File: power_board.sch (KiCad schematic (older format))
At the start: 32 parts, among them CON1 MICROUSB, J1 Conn_02x03_Odd_Even, J2 Conn_01x01, J3 Conn_01x01, J4 Conn_01x01, SW1 SW_Push, U1 PCA9555PW, U2 ATMEGA328P-AU, U3 PCA9555PW, U4 FT232RL, Y1 Crystal

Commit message: Added capacitor references
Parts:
- C1, C10, C2, C5, C6, C7, C8, C9: manf# (none) -> EMK107B7104KAHT
- C3, C4: manf# (none) -> C0603C223K4RACTU
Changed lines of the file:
@@
 F 2 "lsts-passives:C_0603" H 7438 2550 50  0001 C CNN
 F 3 "~" H 7400 2700 50  0001 C CNN
+F 4 "EMK107B7104KAHT" H 7400 2700 50  0001 C CNN "manf#"
 	1    7400 2700
 	-1   0    0    1
@@
 F 2 "lsts-passives:C_0603" H 3788 3050 50  0001 C CNN
 F 3 "~" H 3750 3200 50  0001 C CNN
+F 4 "EMK107B7104KAHT" H 3750 3200 50  0001 C CNN "manf#"
 	1    3750 3200
 	1    0    0    -1
@@
 F 2 "lsts-passives:C_0603" H 3838 1850 50  0001 C CNN
 F 3 "~" H 3800 2000 50  0001 C CNN
+F 4 "C0603C223K4RACTU" H 3800 2000 50  0001 C CNN "manf#"
 	1    3800 2000
 	0    1    1    0
@@
 F 2 "lsts-passives:C_0603" H 3838 2150 50  0001 C CNN
 F 3 "~" H 3800 2300 50  0001 C CNN
+F 4 "C0603C223K4RACTU" H 3800 2300 50  0001 C CNN "manf#"
 	1    3800 2300
 	0    1    1    0
@@
 F 2 "lsts-passives:C_0603" H 8588 950 50  0001 C CNN
 F 3 "~" H 8550 1100 50  0001 C CNN
+F 4 "EMK107B7104KAHT" H 8550 1100 50  0001 C CNN "manf#"
 	1    8550 1100
 	1    0    0    -1
@@
 F 2 "lsts-passives:C_0603" H 4188 3050 50  0001 C CNN
 F 3 "~" H 4150 3200 50  0001 C CNN
+F 4 "EMK107B7104KAHT" H 4150 3200 50  0001 C CNN "manf#"
 	1    4150 3200
 	1    0    0    -1
@@
 F 2 "lsts-passives:C_0603" H 4588 3050 50  0001 C CNN
 F 3 "~" H 4550 3200 50  0001 C CNN
+F 4 "EMK107B7104KAHT" H 4550 3200 50  0001 C CNN "manf#"
 	1    4550 3200
 	1    0    0    -1
@@
 F 2 "lsts-passives:C_0603" H 7838 2550 50  0001 C CNN
 F 3 "~" H 7800 2700 50  0001 C CNN
+F 4 "EMK107B7104KAHT" H 7800 2700 50  0001 C CNN "manf#"
 	1    7800 2700
 	-1   0    0    1
@@
 F 2 "lsts-passives:C_0603" H 2088 4650 50  0001 C CNN
 F 3 "~" H 2050 4800 50  0001 C CNN
+F 4 "EMK107B7104KAHT" H 2050 4800 50  0001 C CNN "manf#"
 	1    2050 4800
 	0    1    1    0
@@
 F 2 "lsts-passives:C_0603" H 4588 4650 50  0001 C CNN
 F 3 "~" H 4550 4800 50  0001 C CNN
+F 4 "EMK107B7104KAHT" H 4550 4800 50  0001 C CNN "manf#"
 	1    4550 4800
 	0    1    1    0

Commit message: Added remaining 0603 references
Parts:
- D1, D2, D3: manf# (none) -> IN-S63AT5G
- R1, R2, R3, R4: manf# (none) -> CRCW060310K0JNEBC
- R5, R6, R7: manf# (none) -> CRCW06031K00FKEAC
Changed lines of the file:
@@
 F 2 "LED_SMD:LED_0603_1608Metric" H 10550 2850 50  0001 C CNN
 F 3 "~" H 10550 2850 50  0001 C CNN
+F 4 "IN-S63AT5G" H 10550 2850 50  0001 C CNN "manf#"
 	1    10550 2850
 	0    1    1    0
@@
 F 2 "LED_SMD:LED_0603_1608Metric" H 10950 2850 50  0001 C CNN
 F 3 "~" H 10950 2850 50  0001 C CNN
+F 4 "IN-S63AT5G" H 10950 2850 50  0001 C CNN "manf#"
 	1    10950 2850
 	0    1    1    0
@@
 F 2 "lsts-passives:R_0603" V 10480 3250 50  0001 C CNN
 F 3 "~" H 10550 3250 50  0001 C CNN
+F 4 "CRCW06031K00FKEAC" H 10550 3250 50  0001 C CNN "manf#"
 	1    10550 3250
 	-1   0    0    1
@@
 F 2 "lsts-passives:R_0603" V 10880 3250 50  0001 C CNN
 F 3 "~" H 10950 3250 50  0001 C CNN
+F 4 "CRCW06031K00FKEAC" H 10950 3250 50  0001 C CNN "manf#"
 	1    10950 3250
 	-1   0    0    1
@@
 F 2 "lsts-passives:R_0603" V 3030 850 50  0001 C CNN
 F 3 "~" H 3100 850 50  0001 C CNN
+F 4 "CRCW060310K0JNEBC" H 3100 850 50  0001 C CNN "manf#"
 	1    3100 850
 	0    1    1    0
@@
 F 2 "lsts-passives:R_0603" V 3680 6400 50  0001 C CNN
 F 3 "~" H 3750 6400 50  0001 C CNN
+F 4 "CRCW060310K0JNEBC" H 3750 6400 50  0001 C CNN "manf#"
 	1    3750 6400
 	-1   0    0    1
@@
 F 2 "lsts-passives:R_0603" V 1080 4950 50  0001 C CNN
 F 3 "~" H 1150 4950 50  0001 C CNN
+F 4 "CRCW060310K0JNEBC" H 1150 4950 50  0001 C CNN "manf#"
 	1    1150 4950
 	-1   0    0    1
@@
 F 2 "lsts-passives:R_0603" V 880 4950 50  0001 C CNN
 F 3 "~" H 950 4950 50  0001 C CNN
+F 4 "CRCW060310K0JNEBC" H 950 4950 50  0001 C CNN "manf#"
 	1    950  4950
 	-1   0    0    1
@@
 F 2 "LED_SMD:LED_0603_1608Metric" H 4950 3450 50  0001 C CNN
 F 3 "~" H 4950 3450 50  0001 C CNN
+F 4 "IN-S63AT5G" H 4950 3450 50  0001 C CNN "manf#"
 	1    4950 3450
 	0    -1   -1   0
@@
 F 2 "lsts-passives:R_0603" V 4880 3050 50  0001 C CNN
 F 3 "~" H 4950 3050 50  0001 C CNN
+F 4 "CRCW06031K00FKEAC" H 4950 3050 50  0001 C CNN "manf#"
 	1    4950 3050
 	1    0    0    -1

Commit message: Changed "out of stock" references.
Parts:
- D1, D2, D3: manf# IN-S63AT5G -> 150060VS75000
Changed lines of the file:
@@
 F 2 "LED_SMD:LED_0603_1608Metric" H 10550 2850 50  0001 C CNN
 F 3 "~" H 10550 2850 50  0001 C CNN
-F 4 "IN-S63AT5G" H 10550 2850 50  0001 C CNN "manf#"
+F 4 "150060VS75000" H 10550 2850 50  0001 C CNN "manf#"
 	1    10550 2850
 	0    1    1    0
@@
 F 2 "LED_SMD:LED_0603_1608Metric" H 10950 2850 50  0001 C CNN
 F 3 "~" H 10950 2850 50  0001 C CNN
-F 4 "IN-S63AT5G" H 10950 2850 50  0001 C CNN "manf#"
+F 4 "150060VS75000" H 10950 2850 50  0001 C CNN "manf#"
 	1    10950 2850
 	0    1    1    0
@@
 F 2 "LED_SMD:LED_0603_1608Metric" H 4950 3450 50  0001 C CNN
 F 3 "~" H 4950 3450 50  0001 C CNN
-F 4 "IN-S63AT5G" H 4950 3450 50  0001 C CNN "manf#"
+F 4 "150060VS75000" H 4950 3450 50  0001 C CNN "manf#"
 	1    4950 3450
 	0    -1   -1   0

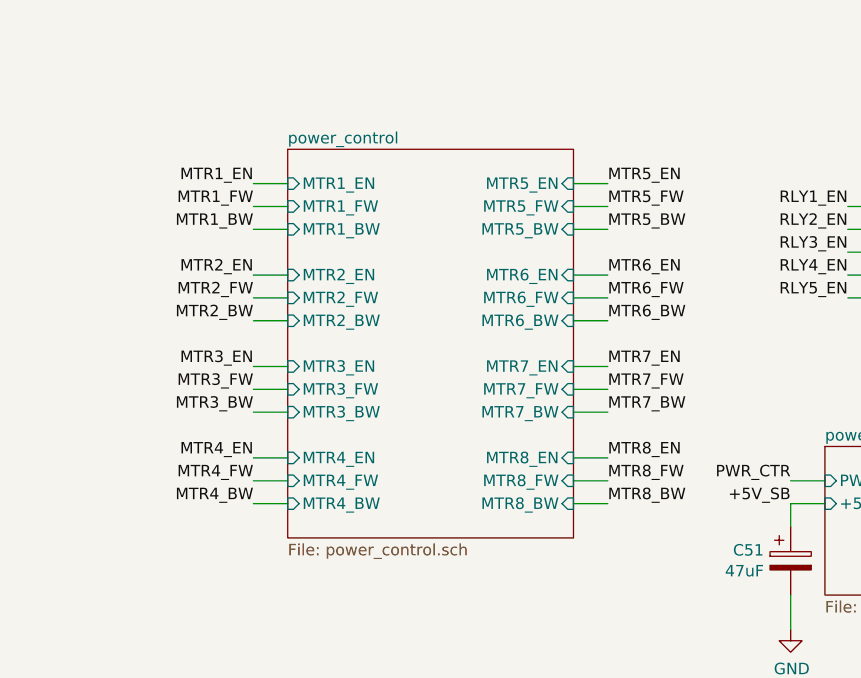
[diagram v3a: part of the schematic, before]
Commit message: Removed L6203
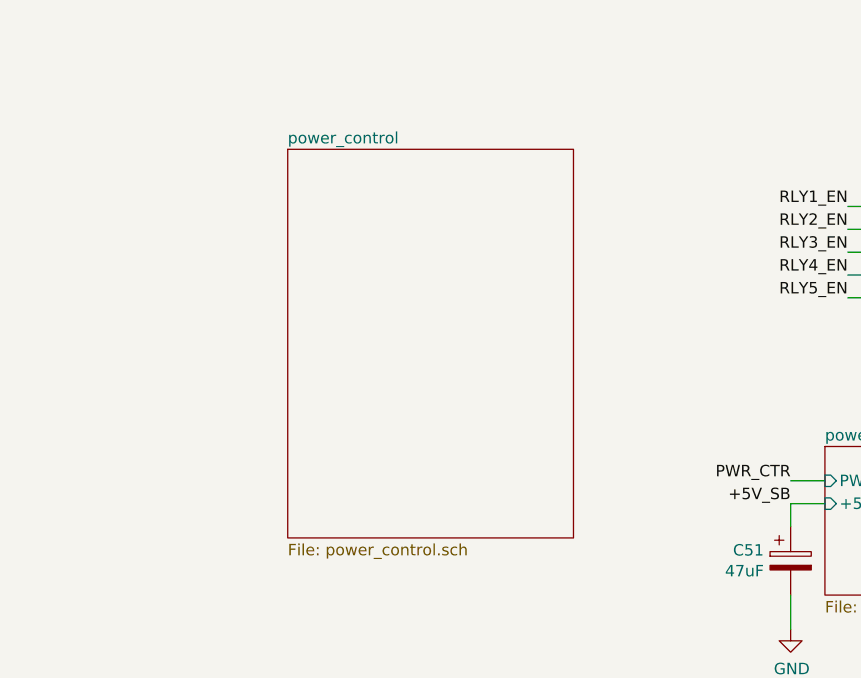
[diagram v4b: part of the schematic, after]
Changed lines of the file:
@@
 +5V_SB
-Wire Wire Line
-	7350 4600 7200 4600
-Wire Wire Line
-	7350 4700 7200 4700
-Wire Wire Line
-	7350 4800 7200 4800
-Wire Wire Line
-	7350 5000 7200 5000
-Wire Wire Line
-	7350 5100 7200 5100
-Wire Wire Line
-	7350 5200 7200 5200
-Wire Wire Line
-	7350 5400 7200 5400
-Wire Wire Line
-	7350 5500 7200 5500
-Wire Wire Line
-	7350 5600 7200 5600
-Wire Wire Line
-	7350 5800 7200 5800
-Wire Wire Line
-	7350 5900 7200 5900
-Wire Wire Line
-	7350 6000 7200 6000
-Wire Wire Line
-	8600 4600 8750 4600
-Wire Wire Line
-	8600 4700 8750 4700
-Wire Wire Line
-	8600 4800 8750 4800
-Text Label 7200 4600 2    50   ~ 0
-MTR1_EN
-Text Label 7200 4700 2    50   ~ 0
-MTR1_FW
-Text Label 7200 4800 2    50   ~ 0
-MTR1_BW
 Wire Wire Line
 	9950 4700 9800 4700
@@
 Text Label 2400 5800 0    50   ~ 0
 MTR1_BW
-Text Label 7200 5000 2    50   ~ 0
-MTR2_EN
-Text Label 7200 5400 2    50   ~ 0
-MTR3_EN
-Text Label 7200 5800 2    50   ~ 0
-MTR4_EN
-Text Label 8750 4600 0    50   ~ 0
-MTR5_EN
-Text Label 7200 5100 2    50   ~ 0
-MTR2_FW
-Text Label 7200 5200 2    50   ~ 0
-MTR2_BW
-Text Label 7200 5500 2    50   ~ 0
-MTR3_FW
-Text Label 7200 5600 2    50   ~ 0
-MTR3_BW
-Text Label 7200 5900 2    50   ~ 0
-MTR4_FW
-Text Label 7200 6000 2    50   ~ 0
-MTR4_BW
-Text Label 8750 4700 0    50   ~ 0
-MTR5_FW
-Text Label 8750 4800 0    50   ~ 0
-MTR5_BW
 Text Label 9800 4700 2    50   ~ 0
 RLY1_EN
@@
 F6 "RLY3_EN" I L 9950 4900 50
 $EndSheet
-$Sheet
-S 7350 4450 1250 1700
-U 5E1C04CF
-F0 "power_control" 50
-F1 "power_control.sch" 50
-F2 "MTR4_EN" I L 7350 5800 50
-F3 "MTR4_FW" I L 7350 5900 50
-F4 "MTR4_BW" I L 7350 6000 50
-F5 "MTR3_EN" I L 7350 5400 50
-F6 "MTR3_FW" I L 7350 5500 50
-F7 "MTR3_BW" I L 7350 5600 50
-F8 "MTR2_EN" I L 7350 5000 50
-F9 "MTR2_FW" I L 7350 5100 50
-F10 "MTR2_BW" I L 7350 5200 50
-F11 "MTR1_EN" I L 7350 4600 50
-F12 "MTR1_FW" I L 7350 4700 50
-F13 "MTR1_BW" I L 7350 4800 50
-F14 "MTR5_EN" I R 8600 4600 50
-F15 "MTR5_FW" I R 8600 4700 50
-F16 "MTR5_BW" I R 8600 4800 50
-F17 "MTR8_EN" I R 8600 5800 50
-F18 "MTR8_FW" I R 8600 5900 50
-F19 "MTR8_BW" I R 8600 6000 50
-F20 "MTR7_EN" I R 8600 5400 50
-F21 "MTR7_FW" I R 8600 5500 50
-F22 "MTR7_BW" I R 8600 5600 50
-F23 "MTR6_EN" I R 8600 5000 50
-F24 "MTR6_FW" I R 8600 5100 50
-F25 "MTR6_BW" I R 8600 5200 50
-$EndSheet
-Wire Wire Line
-	8600 5000 8750 5000
-Wire Wire Line
-	8600 5100 8750 5100
-Wire Wire Line
-	8600 5200 8750 5200
-Text Label 8750 5000 0    50   ~ 0
-MTR6_EN
-Text Label 8750 5100 0    50   ~ 0
-MTR6_FW
-Text Label 8750 5200 0    50   ~ 0
-MTR6_BW
-Wire Wire Line
-	8600 5400 8750 5400
-Wire Wire Line
-	8600 5500 8750 5500
-Wire Wire Line
-	8600 5600 8750 5600
-Text Label 8750 5400 0    50   ~ 0
-MTR7_EN
-Text Label 8750 5500 0    50   ~ 0
-MTR7_FW
-Text Label 8750 5600 0    50   ~ 0
-MTR7_BW
-Wire Wire Line
-	8600 5800 8750 5800
-Wire Wire Line
-	8600 5900 8750 5900
-Wire Wire Line
-	8600 6000 8750 6000
-Text Label 8750 5800 0    50   ~ 0
-MTR8_EN
-Text Label 8750 5900 0    50   ~ 0
-MTR8_FW
-Text Label 8750 6000 0    50   ~ 0
-MTR8_BW
 NoConn ~ 10250 1600
 NoConn ~ 10250 1800
@@
 	1    0    0    -1
 $EndComp
+$Sheet
+S 7350 4450 1250 1700
+U 5E1C04CF
+F0 "power_control" 50
+F1 "power_control.sch" 50
+$EndSheet
 $EndSCHEMATC

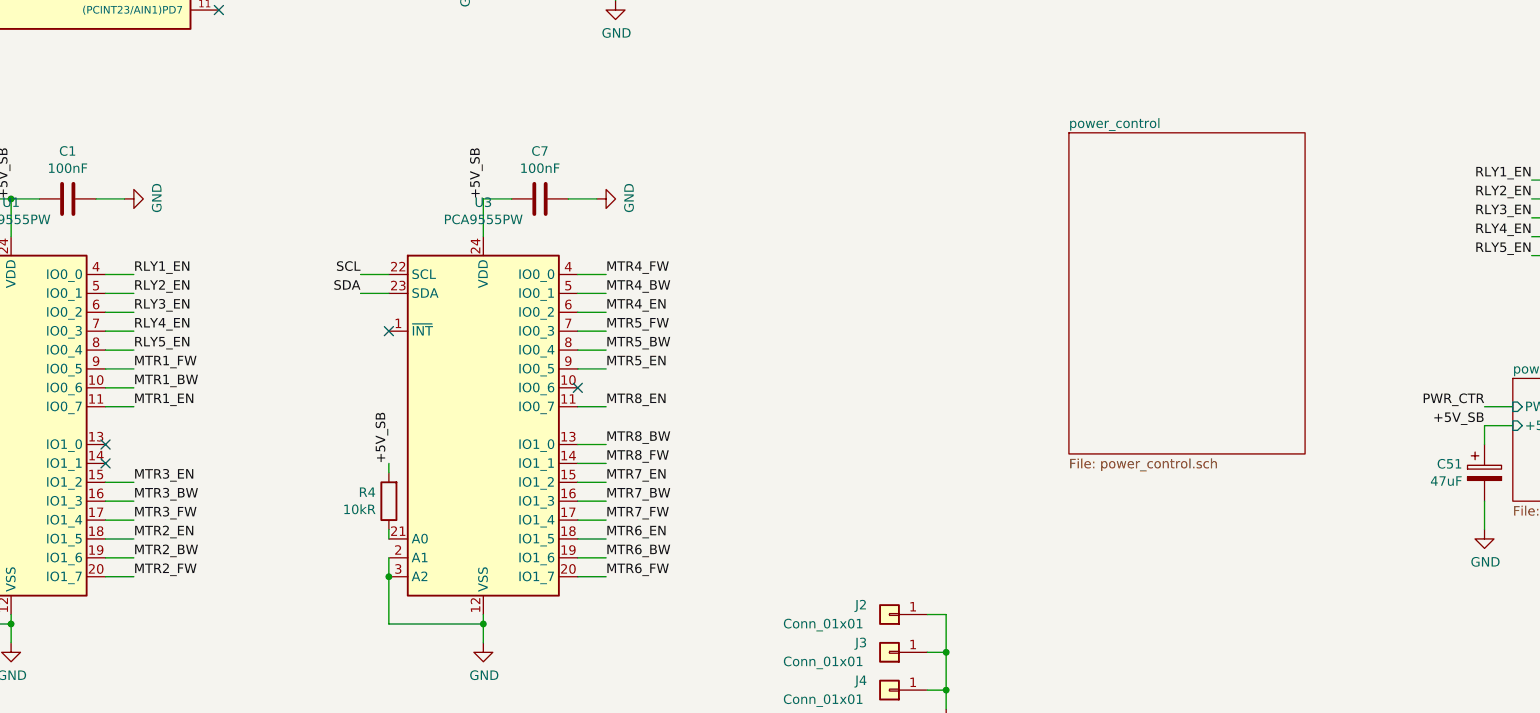
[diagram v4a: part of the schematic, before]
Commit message: Added DRV8801PWP to schematic
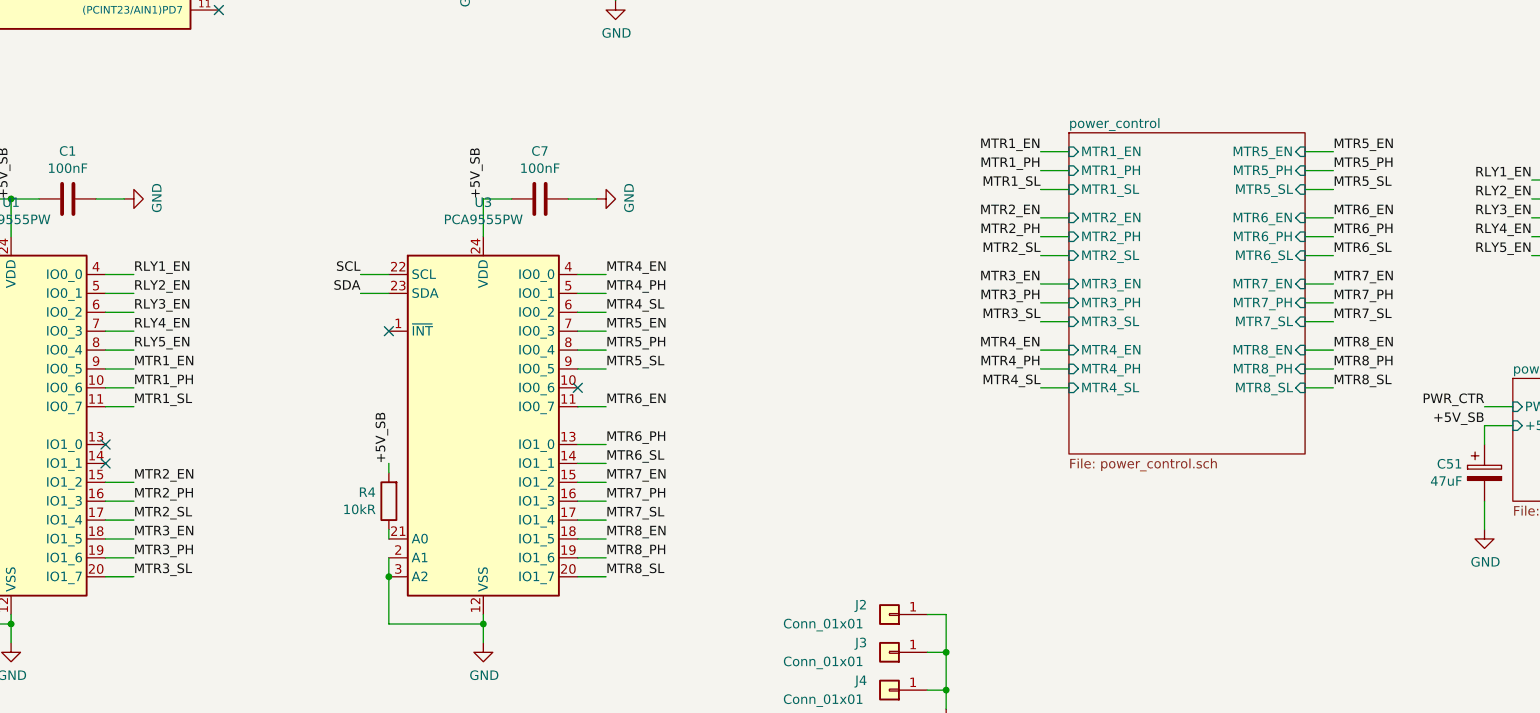
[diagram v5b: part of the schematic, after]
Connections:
- net MTR1_FW is gone; now on net MTR1_EN: U1.9 (IO0_5)
- net MTR4_FW is gone; now on net MTR4_EN: U3.4 (IO0_0)
- net MTR5_FW is gone; now on net MTR5_EN: U3.7 (IO0_3)
- net MTR1_EN: no longer U1.11 (IO0_7)
- net MTR2_EN: now also U1.15 (IO1_2); no longer U1.18 (IO1_5)
- net MTR3_EN: now also U1.18 (IO1_5); no longer U1.15 (IO1_2)
- net MTR4_EN: no longer U3.6 (IO0_2)
- net MTR5_EN: no longer U3.9 (IO0_5)
- net MTR6_EN: now also U3.11 (IO0_7); no longer U3.18 (IO1_5)
- net MTR8_EN: now also U3.18 (IO1_5); no longer U3.11 (IO0_7)
- net MTR1_BW renamed MTR1_PH
- net MTR2_BW renamed MTR3_PH
- net MTR2_FW renamed MTR3_SL
- net MTR3_BW renamed MTR2_PH
- net MTR3_FW renamed MTR2_SL
- net MTR4_BW renamed MTR4_PH
- net MTR5_BW renamed MTR5_PH
- net MTR6_BW renamed MTR8_PH
- net MTR6_FW renamed MTR8_SL
- net MTR7_BW renamed MTR7_PH
- net MTR7_FW renamed MTR7_SL
- net MTR8_BW renamed MTR6_PH
- net MTR8_FW renamed MTR6_SL
- new net MTR1_SL: U1.11 (IO0_7)
- new net MTR4_SL: U3.6 (IO0_2)
- new net MTR5_SL: U3.9 (IO0_5)
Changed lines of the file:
@@
 Wire Wire Line
 	2250 5600 2400 5600
-Text Label 2400 5900 0    50   ~ 0
-MTR1_EN
-Text Label 2400 5700 0    50   ~ 0
-MTR1_FW
-Text Label 2400 5800 0    50   ~ 0
-MTR1_BW
 Text Label 9800 4700 2    50   ~ 0
 RLY1_EN
@@
 Text Label 9800 5100 2    50   ~ 0
 RLY5_EN
-Text Label 2400 6600 0    50   ~ 0
-MTR2_EN
-Text Label 2400 6700 0    50   ~ 0
-MTR2_BW
-Text Label 2400 6300 0    50   ~ 0
-MTR3_EN
-Text Label 2400 6500 0    50   ~ 0
-MTR3_FW
-Text Label 4900 5400 0    50   ~ 0
-MTR4_EN
-Text Label 4900 5200 0    50   ~ 0
-MTR4_FW
-Text Label 4900 5300 0    50   ~ 0
-MTR4_BW
-Text Label 4900 5700 0    50   ~ 0
-MTR5_EN
-Text Label 4900 5500 0    50   ~ 0
-MTR5_FW
-Text Label 4900 5600 0    50   ~ 0
-MTR5_BW
 Text Label 2400 5200 0    50   ~ 0
 RLY1_EN
@@
 Wire Wire Line
 	4750 6600 4900 6600
-Text Label 4900 6600 0    50   ~ 0
-MTR6_EN
-Text Label 4900 6800 0    50   ~ 0
-MTR6_FW
-Text Label 4900 6700 0    50   ~ 0
-MTR6_BW
 Wire Wire Line
 	4750 5900 4900 5900
@@
 Wire Wire Line
 	4750 6200 4900 6200
-Text Label 4900 6300 0    50   ~ 0
-MTR7_EN
-Text Label 4900 6500 0    50   ~ 0
-MTR7_FW
-Text Label 4900 6400 0    50   ~ 0
-MTR7_BW
 Wire Wire Line
 	4750 6300 4900 6300
@@
 Wire Wire Line
 	4750 6500 4900 6500
-Text Label 4900 5900 0    50   ~ 0
-MTR8_EN
-Text Label 4900 6200 0    50   ~ 0
-MTR8_FW
-Text Label 4900 6100 0    50   ~ 0
-MTR8_BW
 Wire Wire Line
 	950  1200 950  1500
@@
 NoConn ~ 2250 6100
 NoConn ~ 2250 6200
-Text Label 2400 6800 0    50   ~ 0
-MTR2_FW
 Wire Wire Line
 	2250 6800 2400 6800
-Text Label 2400 6400 0    50   ~ 0
-MTR3_BW
 Wire Wire Line
 	2250 6400 2400 6400
@@
 F0 "power_control" 50
 F1 "power_control.sch" 50
+F2 "MTR1_EN" I L 7350 4550 50
+F3 "MTR1_PH" I L 7350 4650 50
+F4 "MTR1_SL" I L 7350 4750 50
+F5 "MTR2_EN" I L 7350 4900 50
+F6 "MTR2_PH" I L 7350 5000 50
+F7 "MTR2_SL" I L 7350 5100 50
+F8 "MTR3_EN" I L 7350 5250 50
+F9 "MTR3_PH" I L 7350 5350 50
+F10 "MTR3_SL" I L 7350 5450 50
+F11 "MTR4_EN" I L 7350 5600 50
+F12 "MTR4_PH" I L 7350 5700 50
+F13 "MTR4_SL" I L 7350 5800 50
+F14 "MTR5_EN" I R 8600 4550 50
+F15 "MTR5_PH" I R 8600 4650 50
+F16 "MTR5_SL" I R 8600 4750 50
+F17 "MTR6_EN" I R 8600 4900 50
+F18 "MTR6_PH" I R 8600 5000 50
+F19 "MTR6_SL" I R 8600 5100 50
+F20 "MTR7_EN" I R 8600 5250 50
+F21 "MTR7_PH" I R 8600 5350 50
+F22 "MTR7_SL" I R 8600 5450 50
+F23 "MTR8_EN" I R 8600 5600 50
+F24 "MTR8_PH" I R 8600 5700 50
+F25 "MTR8_SL" I R 8600 5800 50
 $EndSheet
+Wire Wire Line
+	7350 4550 7200 4550
+Wire Wire Line
+	7350 4650 7200 4650
+Wire Wire Line
+	7350 4750 7200 4750
+Wire Wire Line
+	7350 4900 7200 4900
+Wire Wire Line
+	7350 5000 7200 5000
+Wire Wire Line
+	7350 5100 7200 5100
+Wire Wire Line
+	7350 5250 7200 5250
+Wire Wire Line
+	7350 5350 7200 5350
+Wire Wire Line
+	7350 5450 7200 5450
+Wire Wire Line
+	7350 5600 7200 5600
+Wire Wire Line
+	7350 5700 7200 5700
+Wire Wire Line
+	7350 5800 7200 5800
+Wire Wire Line
+	8750 4550 8600 4550
+Wire Wire Line
+	8750 4650 8600 4650
+Wire Wire Line
+	8750 4750 8600 4750
+Wire Wire Line
+	8750 4900 8600 4900
+Wire Wire Line
+	8750 5000 8600 5000
+Wire Wire Line
+	8750 5100 8600 5100
+Wire Wire Line
+	8750 5250 8600 5250
+Wire Wire Line
+	8750 5350 8600 5350
+Wire Wire Line
+	8750 5450 8600 5450
+Wire Wire Line
+	8750 5600 8600 5600
+Wire Wire Line
+	8750 5700 8600 5700
+Wire Wire Line
+	8750 5800 8600 5800
+Text Label 7200 4550 2    50   ~ 0
+MTR1_EN
+Text Label 7200 4650 2    50   ~ 0
+MTR1_PH
+Text Label 7200 4750 2    50   ~ 0
+MTR1_SL
+Text Label 7200 4900 2    50   ~ 0
+MTR2_EN
+Text Label 7200 5000 2    50   ~ 0
+MTR2_PH
+Text Label 7200 5100 2    50   ~ 0
+MTR2_SL
+Text Label 7200 5250 2    50   ~ 0
+MTR3_EN
+Text Label 7200 5350 2    50   ~ 0
+MTR3_PH
+Text Label 7200 5450 2    50   ~ 0
+MTR3_SL
+Text Label 7200 5600 2    50   ~ 0
+MTR4_EN
+Text Label 7200 5700 2    50   ~ 0
+MTR4_PH
+Text Label 7200 5800 2    50   ~ 0
+MTR4_SL
+Text Label 8750 4900 0    50   ~ 0
+MTR6_EN
+Text Label 8750 5000 0    50   ~ 0
+MTR6_PH
+Text Label 8750 5100 0    50   ~ 0
+MTR6_SL
+Text Label 8750 5250 0    50   ~ 0
+MTR7_EN
+Text Label 8750 5350 0    50   ~ 0
+MTR7_PH
+Text Label 8750 5450 0    50   ~ 0
+MTR7_SL
+Text Label 8750 5600 0    50   ~ 0
+MTR8_EN
+Text Label 8750 5700 0    50   ~ 0
+MTR8_PH
+Text Label 8750 5800 0    50   ~ 0
+MTR8_SL
+Text Label 2400 5700 0    50   ~ 0
+MTR1_EN
+Text Label 2400 5800 0    50   ~ 0
+MTR1_PH
+Text Label 2400 5900 0    50   ~ 0
+MTR1_SL
+Text Label 2400 6300 0    50   ~ 0
+MTR2_EN
+Text Label 2400 6400 0    50   ~ 0
+MTR2_PH
+Text Label 2400 6500 0    50   ~ 0
+MTR2_SL
+Text Label 2400 6600 0    50   ~ 0
+MTR3_EN
+Text Label 8750 4750 0    50   ~ 0
+MTR5_SL
+Text Label 8750 4650 0    50   ~ 0
+MTR5_PH
+Text Label 8750 4550 0    50   ~ 0
+MTR5_EN
+Text Label 2400 6700 0    50   ~ 0
+MTR3_PH
+Text Label 2400 6800 0    50   ~ 0
+MTR3_SL
+Text Label 4900 5900 0    50   ~ 0
+MTR6_EN
+Text Label 4900 6100 0    50   ~ 0
+MTR6_PH
+Text Label 4900 6200 0    50   ~ 0
+MTR6_SL
+Text Label 4900 6300 0    50   ~ 0
+MTR7_EN
+Text Label 4900 6400 0    50   ~ 0
+MTR7_PH
+Text Label 4900 6500 0    50   ~ 0
+MTR7_SL
+Text Label 4900 6600 0    50   ~ 0
+MTR8_EN
+Text Label 4900 6700 0    50   ~ 0
+MTR8_PH
+Text Label 4900 6800 0    50   ~ 0
+MTR8_SL
+Text Label 4900 5700 0    50   ~ 0
+MTR5_SL
+Text Label 4900 5600 0    50   ~ 0
+MTR5_PH
+Text Label 4900 5500 0    50   ~ 0
+MTR5_EN
+Text Label 4900 5200 0    50   ~ 0
+MTR4_EN
+Text Label 4900 5300 0    50   ~ 0
+MTR4_PH
+Text Label 4900 5400 0    50   ~ 0
+MTR4_SL
 $EndSCHEMATC
